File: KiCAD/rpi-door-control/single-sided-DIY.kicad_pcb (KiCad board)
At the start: 2 copper layers, 123 x 50 mm, 30 parts, among them IC1 4N35, J1 RJ45, P1 CONN_13X2, P2 CONN_2, P3 CONN_2, P4 CONN_2, Q1 2N3904, Q2 2N3904, SW1 SW_PUSH, U1 RELAY

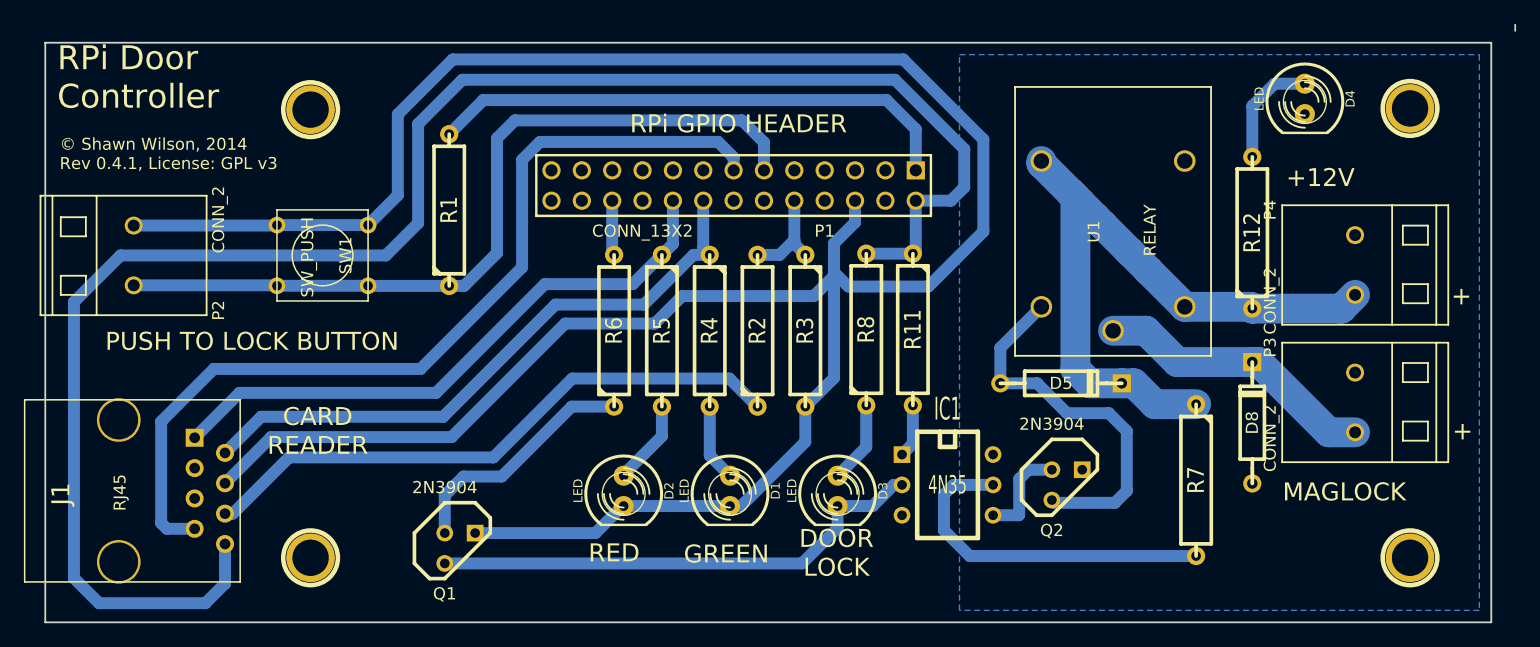
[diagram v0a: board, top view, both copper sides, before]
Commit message: Fixed the backwards transistors and the upside down relay on the door controller pcb
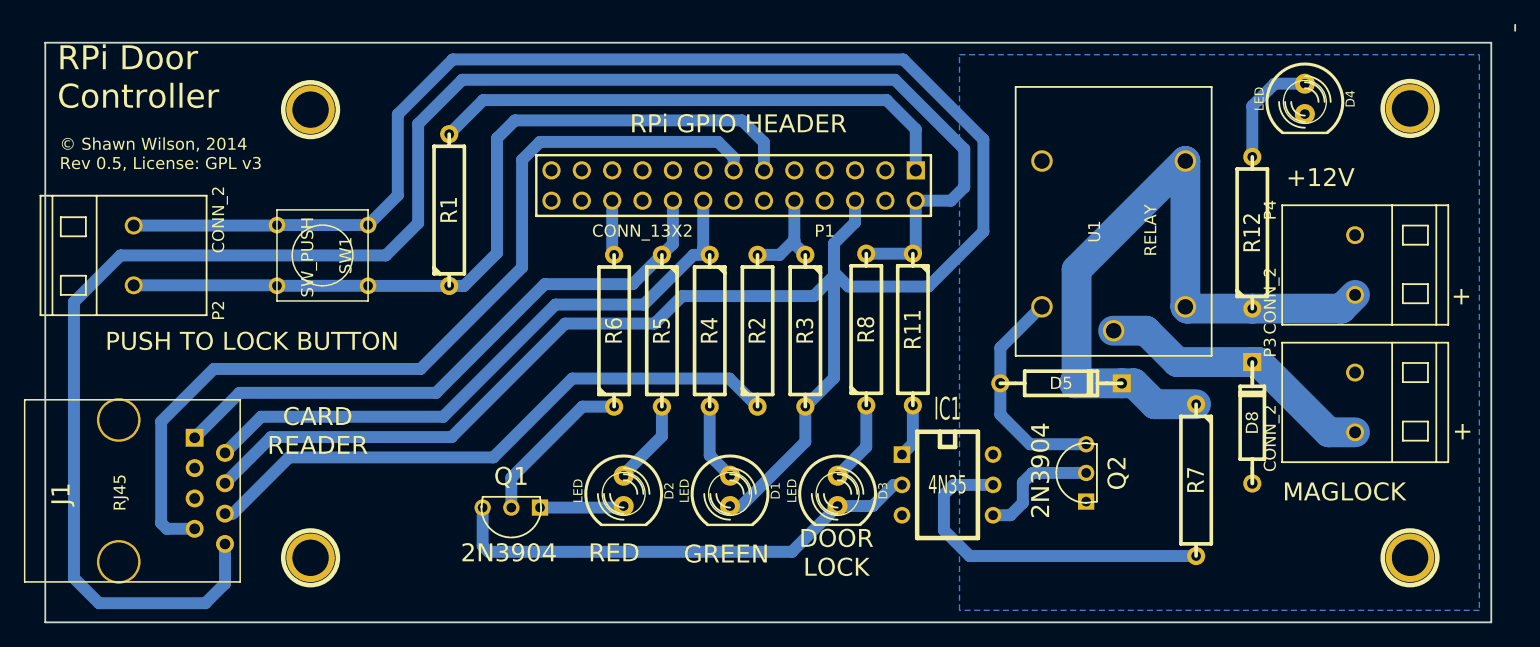
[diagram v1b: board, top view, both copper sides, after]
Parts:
- Q1, Q2: footprint TO92 -> TO92-2N3904
- moved Q1 5.48 mm to (119.0, 116.4), turned to 180 degrees
- moved Q2 1.89 mm to (167.1, 113.5), turned to 90 degrees
- moved U1 0.05 mm to (169.4, 99.6)
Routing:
- net GND: track 219.2 -> 204.0 mm
- net N-0000038: track 31.8 -> 18.6 mm
- net N-000003: track 20.4 -> 13.6 mm
- net +12V: track 58.1 -> 60.3 mm
- net N-0000020: track 8.26 -> 10.3 mm
- net N-0000025: track 42.1 -> 40.8 mm
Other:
- board text added: "© Shawn Wilson, 2014 Rev 0.5, License: GPL v3"
- board text removed: "© Shawn Wilson, 2014 Rev 0.4.1, License: GPL v3"
